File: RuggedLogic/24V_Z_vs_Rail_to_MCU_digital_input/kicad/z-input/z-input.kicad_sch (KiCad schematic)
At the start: 17 parts, among them J1 24V_Z, J2 24V, J3 3V3_OUT, J4 Select, T1 BCP5616Q, U1 APC-817B-SL, U2 OPB616

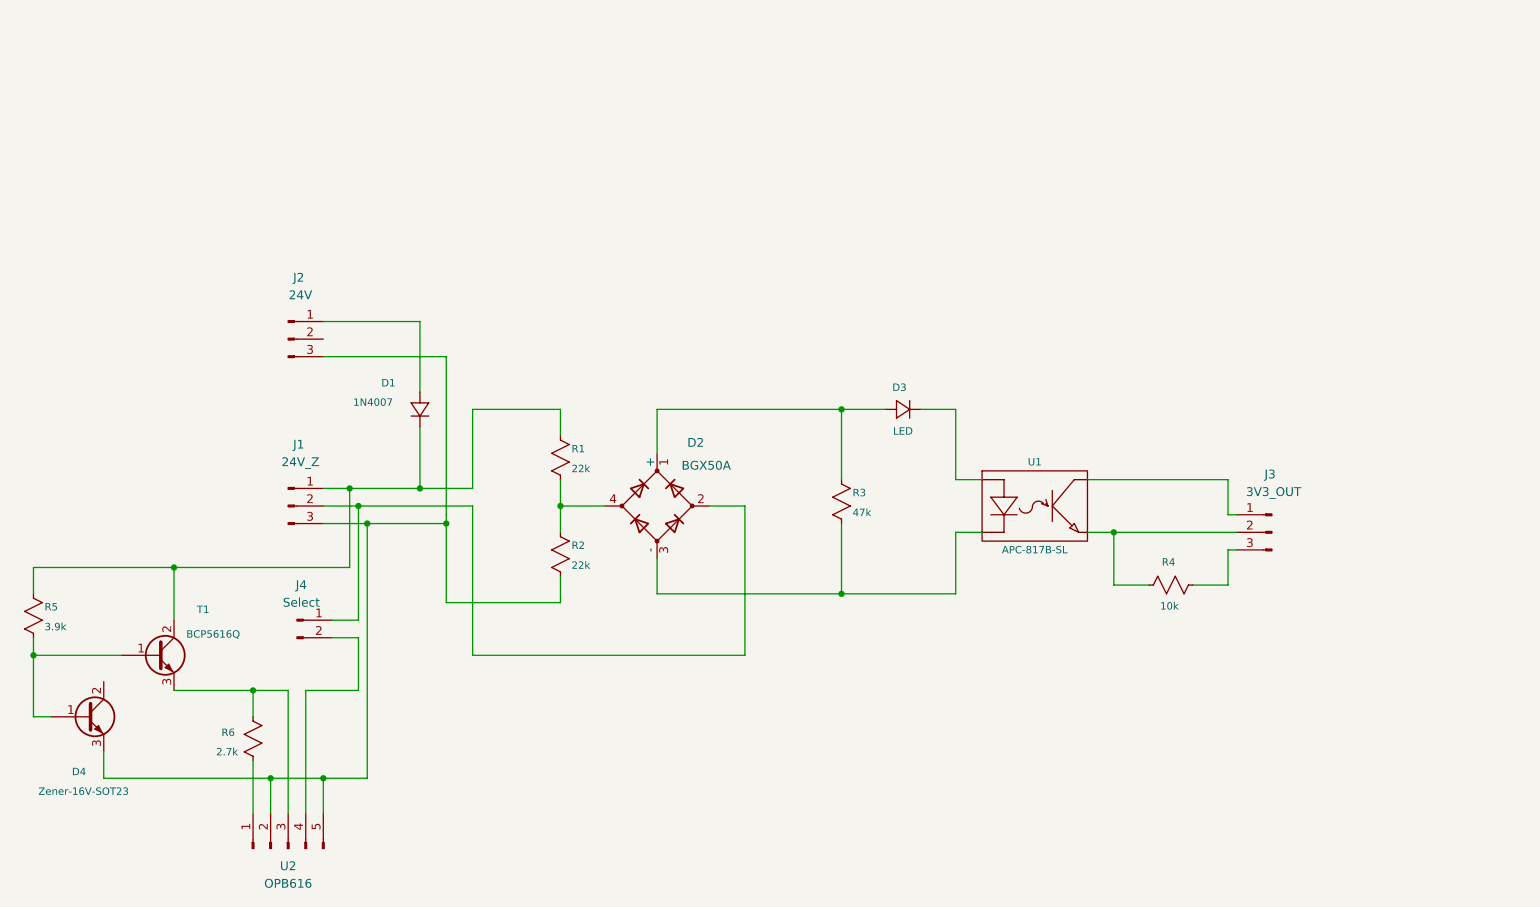
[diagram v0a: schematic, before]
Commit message: Redone Z-input PCB; production update
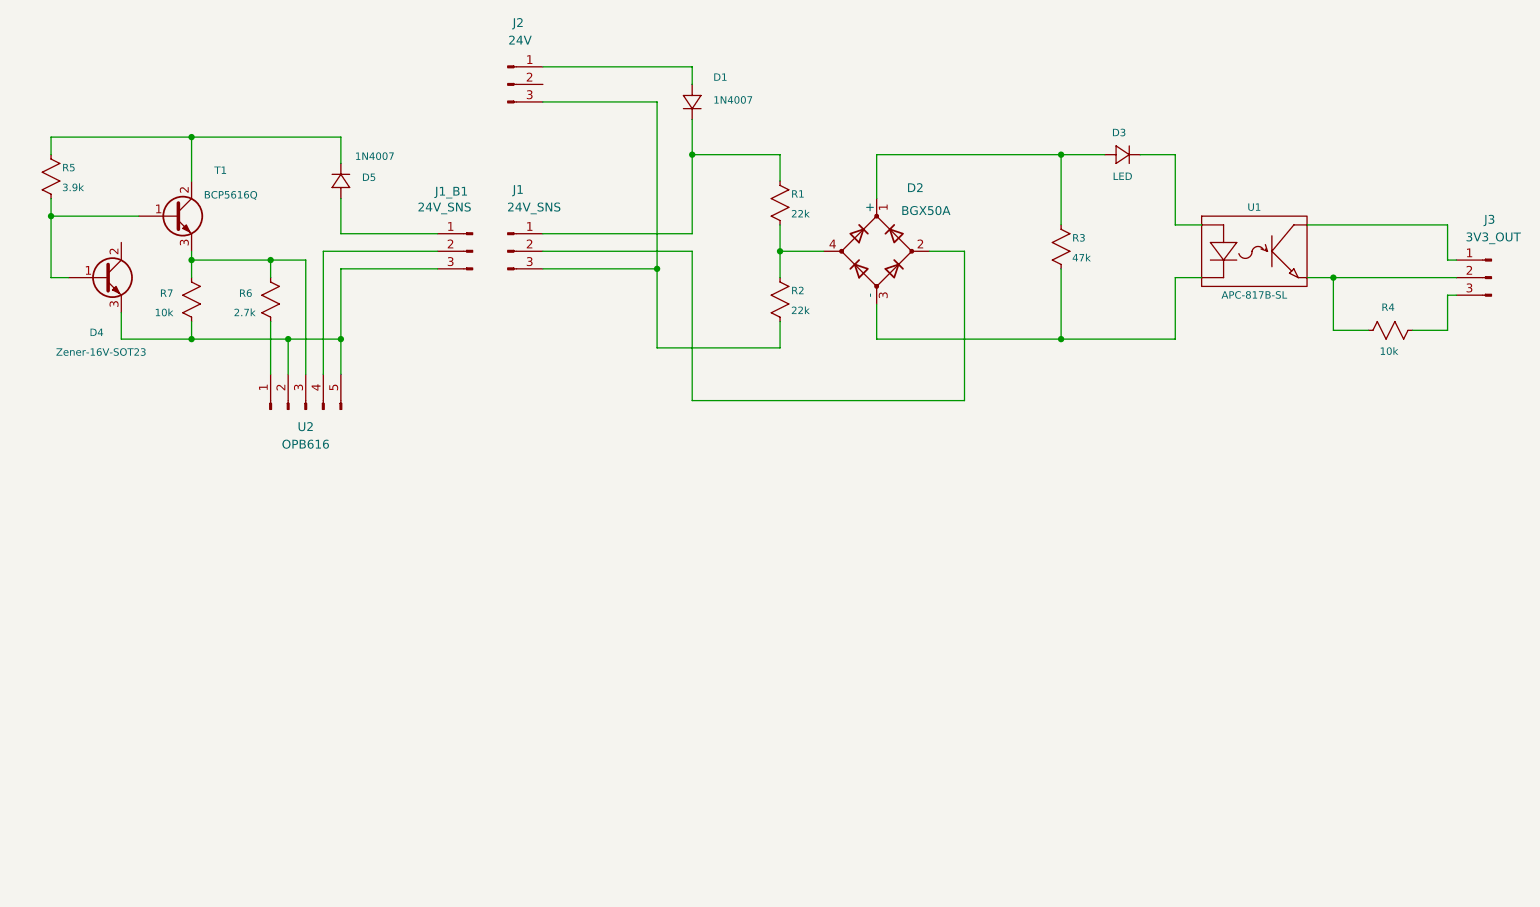
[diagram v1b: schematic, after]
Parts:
- removed J4: Select, Connector_PinHeader_2.54mm:PinHeader_1x02_P2.54mm_Vertical, symbol Connector:Conn_01x02_Pin
- added D5: 1N4007, Secoh:D_SOD-123F_hand_soldering, symbol ltspice:diode
- added J1_B1: 24V_SNS, Connector_Molex:Molex_KK-396_A-41791-0003_1x03_P3.96mm_Vertical, symbol Connector:Conn_01x03_Pin
- added R7: 10k, Resistor_SMD:R_0805_2012Metric_Pad1.20x1.40mm_HandSolder, symbol ltspice:res
- D1: footprint Secoh:D_SOD-123F_inverted_polarity -> Secoh:D_SOD-123F_hand_soldering
- J1: value 24V_Z -> 24V_SNS
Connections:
- net at U2.4 (Pin_4): now also J1_B1.2 (Pin_2)
- net at D4.3 (E), U2.2 (Pin_2), U2.5 (Pin_5): now also J1_B1.3 (Pin_3), R7.2; no longer J1.3 (Pin_3), J2.3 (Pin_3), R2.2
- net at R6.1, T1.3 (E), U2.3 (Pin_3): now also R7.1
- net at D1.2 (-), J1.1 (Pin_1), R1.1: no longer R5.1, T1.2 (C)
- new net: D5.1 (+), J1_B1.1 (Pin_1)
- new net: D5.2 (-), R5.1, T1.2 (C)
- new net: J1.3 (Pin_3), J2.3 (Pin_3), R2.2
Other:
- moved on the sheet: D1, D2, D3, D4, J1, J2, J3, R1, R2, R3, R4, R5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

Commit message: Fixed errors in Rugged Z sensor Fixes to Rugged Switch
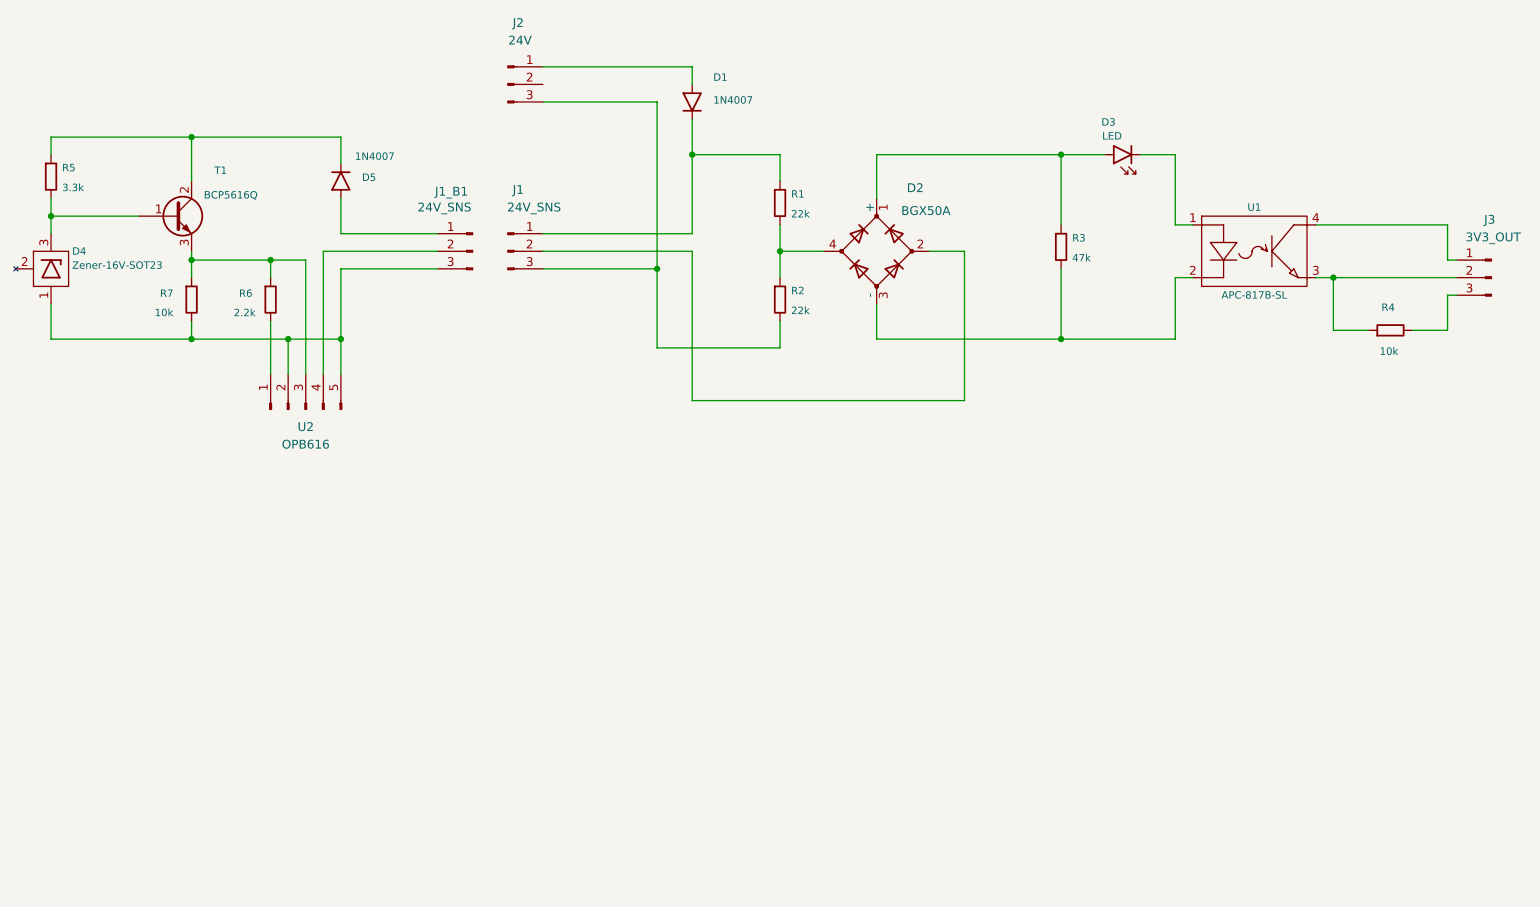
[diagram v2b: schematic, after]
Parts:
- D1, D5: symbol ltspice:diode -> Secoh:SOD-123/Diode
- D3: footprint LED_SMD:LED_0805_2012Metric_Pad1.15x1.40mm_HandSolder -> Secoh:LED_0805; symbol ltspice:diode -> Secoh:0805/LED
- D4: symbol Device:Q_NPN_BCE -> Secoh:Zener/MMBZ52_SOT-23
- R1, R2, R3, R4, R7: symbol ltspice:res -> Secoh:0805/R
- R5: value 3.9k -> 3.3k; symbol ltspice:res -> Secoh:0805/R
- R6: value 2.7k -> 2.2k; symbol ltspice:res -> Secoh:0805/R
- U1: symbol ltspice:Optos/PC817B -> Secoh:Optos/PC817B
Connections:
- net at D2.1 (+), R3.1: now also D3.2 (A); no longer D3.1 (+)
- net at U1.1 (D+): now also D3.1 (K); no longer D3.2 (-)
- net at D5.1 (K): now also R5.1, T1.2 (C); no longer J1_B1.1 (Pin_1)
- net at J1_B1.3 (Pin_3), R7.2, U2.2 (Pin_2)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: now also D4.1 (A); no longer D4.3 (E)
- net at U1.3 (C): now also J3.2 (Pin_2), R4.1; no longer J3.1 (Pin_1)
- net at R5.2, T1.1 (B): now also D4.3 (K); no longer D4.1 (B)
- net at J1.1 (Pin_1), R1.1: now also D1.1 (K); no longer D1.2 (-)
- net at J2.1 (Pin_1): now also D1.2 (A); no longer D1.1 (+)
- new net: D5.2 (A), J1_B1.1 (Pin_1)
- new net: J3.1 (Pin_1), U1.4 (C)
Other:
- moved on the sheet: D3, D4

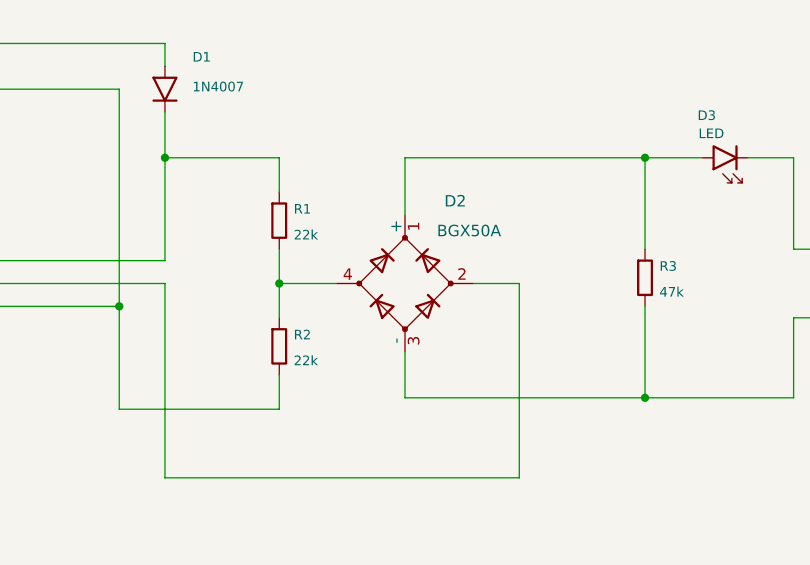
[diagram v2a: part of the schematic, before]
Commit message: Updated Rugged Z sensor and Switch; schematics and PCB
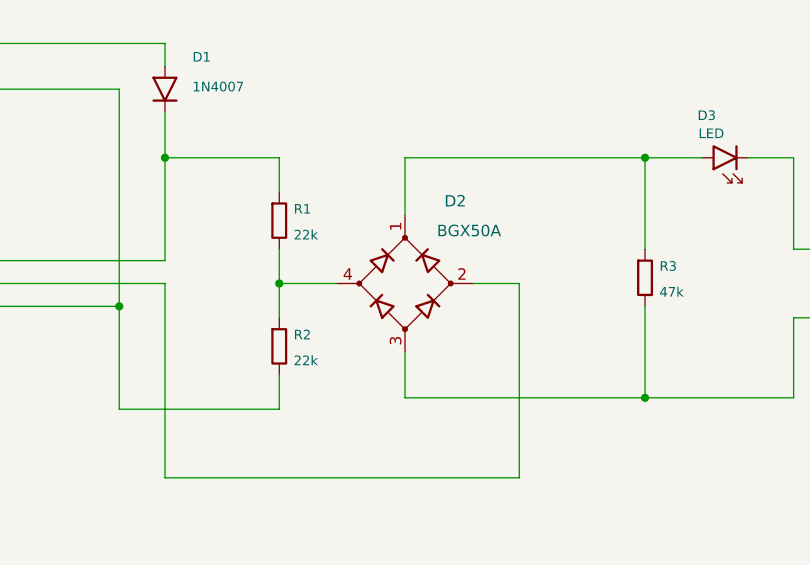
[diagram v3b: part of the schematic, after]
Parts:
- D2: symbol Device:D_Bridge_+A-A -> Secoh:D-Bridge/BGX50A_SOT-143
- T1: symbol Device:Q_NPN_BCE -> Secoh:NPN/BCP5616Q
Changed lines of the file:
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@@
 	)
 	(symbol
-		(lib_id "Device:D_Bridge_+A-A")
+		(lib_id "Secoh:D-Bridge/BGX50A_SOT-143")
 		(at 157.48 73.66 90)
 		(unit 1)
@@
 	)
 	(symbol
-		(lib_id "Device:Q_NPN_BCE")
+		(lib_id "Secoh:NPN/BCP5616Q")
 		(at 55.88 68.58 0)
 		(unit 1)
@@
 		)
 		(property "Footprint" "Package_TO_SOT_SMD:SOT-223-3_TabPin2"
-			(at 60.96 66.04 0)
-			(effects
-				(font
+			(at 57.15 76.2 0)
+			(effects
+				(font
